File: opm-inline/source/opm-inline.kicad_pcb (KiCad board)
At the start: 4 copper layers, 58 x 40 mm, 71 parts, among them IC1 TMC6200-TA, J1 Info, J2 VCC_IO, J3 PWMx6, J4 Fan, J6 Current Sensing, Q1 HYG025N06LS1C2, Q2 HYG025N06LS1C2, Q3 HYG025N06LS1C2, Q4 HYG025N06LS1C2, Q5 HYG025N06LS1C2, Q6 HYG025N06LS1C2, U2 TerminalBlock_2_P5.08mm, U3 TerminalBlock_3_P5.08mm

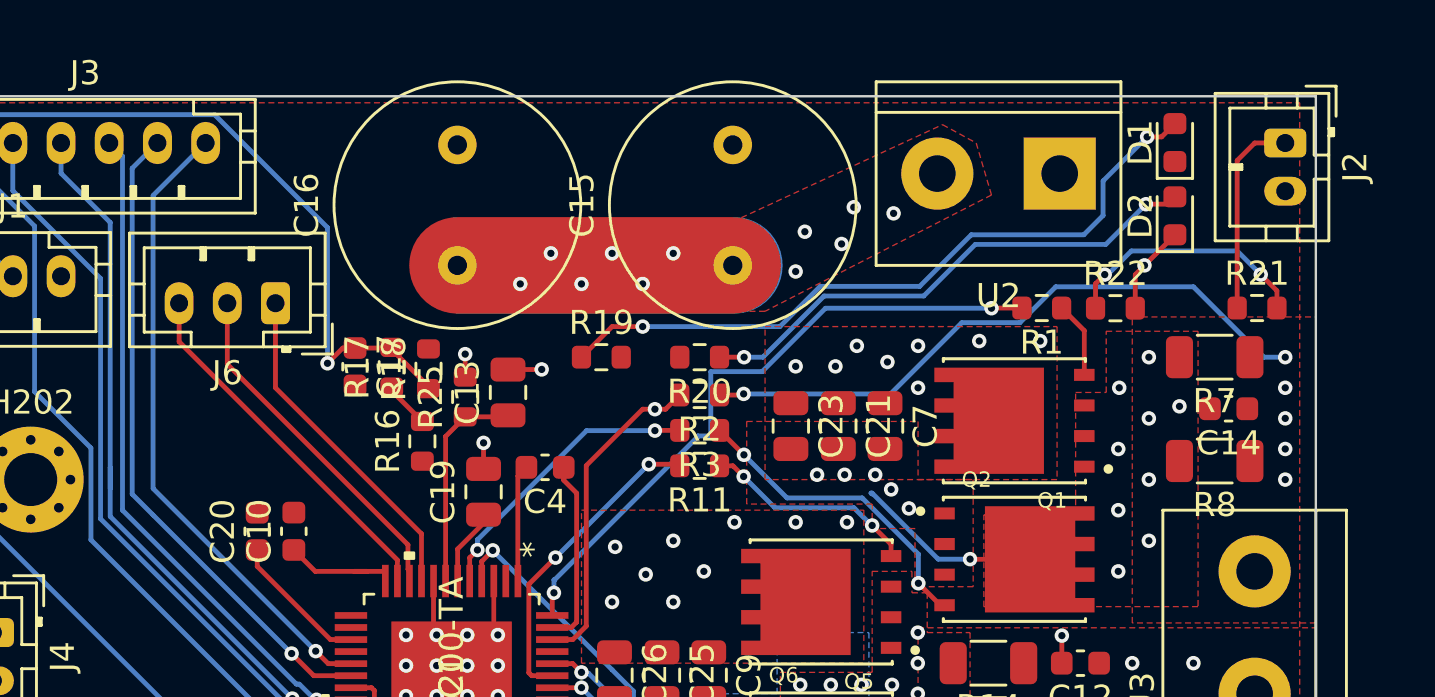
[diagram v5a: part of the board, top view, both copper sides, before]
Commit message: route tracks
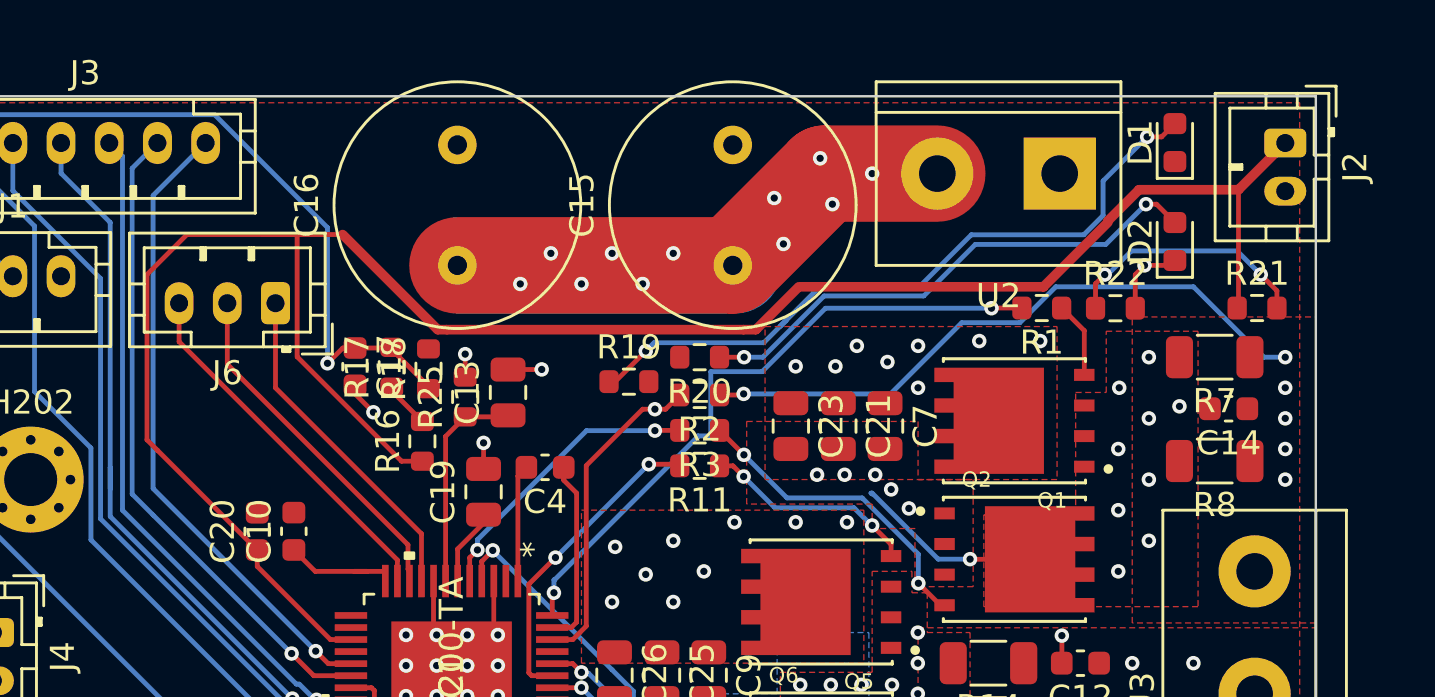
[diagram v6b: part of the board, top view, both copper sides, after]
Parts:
- moved R19 1.53 mm to (159.4, 78.5)
- moved D2 1.07 mm to (182.1, 72.7)
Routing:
- net /+VCC_IO: track 25.9 -> 102.5 mm
- net /+VM: track 71.2 -> 81.3 mm
- net GND: track 23.1 -> 24.1 mm, vias 32 -> 33
- net Net-(D1-Pad2): track 29.7 -> 29.1 mm

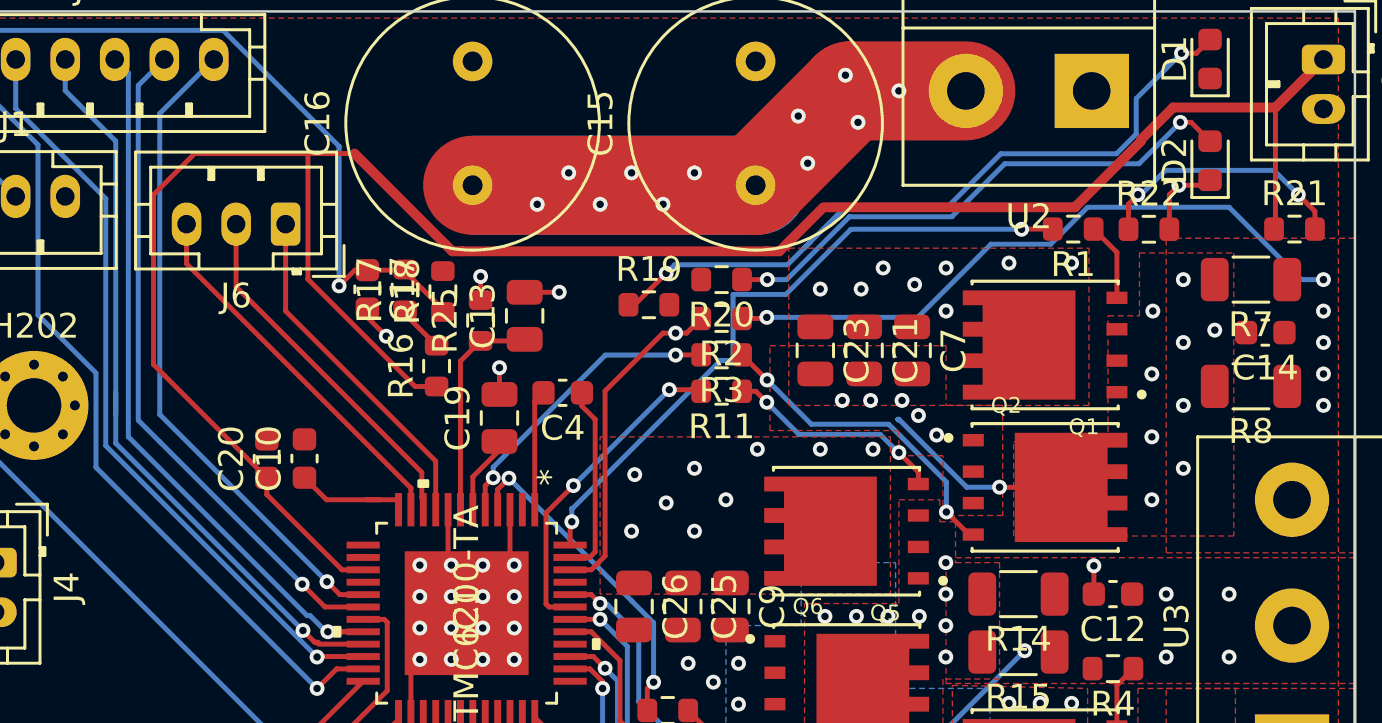
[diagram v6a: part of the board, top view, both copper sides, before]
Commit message: route tracks
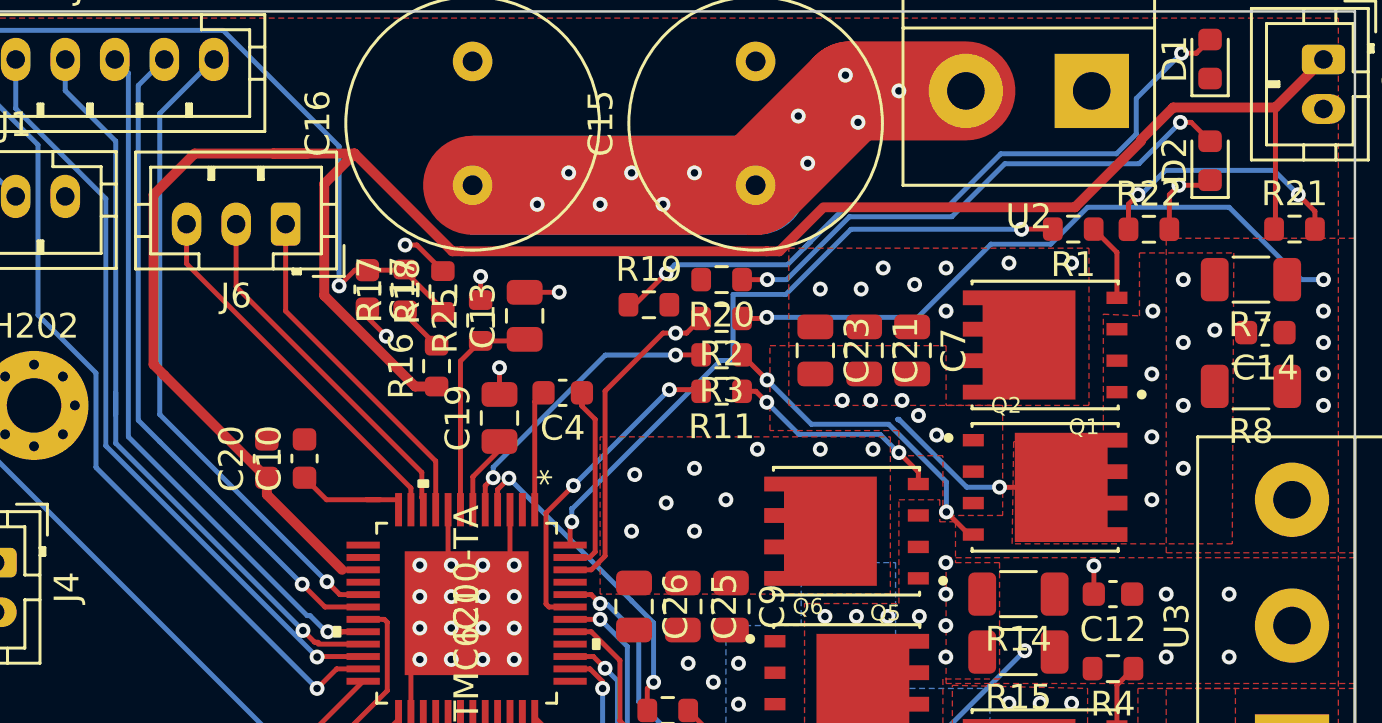
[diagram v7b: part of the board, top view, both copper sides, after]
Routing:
- net GND: track 24.1 -> 26.1 mm, vias 33 -> 34
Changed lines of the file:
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@@
     (thickness 1.6)
     (drawings 4)
-    (tracks 518)
+    (tracks 522)
     (zones 0)
     (modules 71)
@@
   (gr_line (start 187.96 66.64) (end 187.96 106.63) (layer Edge.Cuts) (width 0.1))
   (gr_line (start 187.96 106.63) (end 130.01 106.63) (layer Edge.Cuts) (width 0.1))
+  (via (at 149.606 76.073) (size 0.6) (drill 0.3) (layers F.Cu B.Cu) (net 5))
   (via (at 148.844 79.756) (size 0.6) (drill 0.3) (layers F.Cu B.Cu) (net 5))
   (via (at 185.674 74.041) (size 0.6) (drill 0.3) (layers F.Cu B.Cu) (net 50))
@@
   (segment (start 181.907 73.66) (end 182.11 73.457) (width 0.2) (layer F.Cu) (net 5))
   (segment (start 180.848 73.66) (end 181.907 73.66) (width 0.2) (layer F.Cu) (net 5))
+  (segment (start 150.077 76.073) (end 149.606 76.073) (width 0.2) (layer F.Cu) (net 5))
+  (segment (start 151.13 77.126) (end 150.077 76.073) (width 0.2) (layer F.Cu) (net 5))
   (via (at 146.939 77.724) (size 0.6) (drill 0.3) (layers F.Cu B.Cu) (net 53))
   (via (at 174.498 75.438) (size 0.6) (drill 0.3) (layers F.Cu B.Cu) (net 39))
@@
   (segment (start 179.197 74.041) (end 179.324 74.041) (width 0.2) (layer B.Cu) (net 50))
   (segment (start 147.9117 89.190001) (end 147.0589 89.190001) (width 0.2) (layer F.Cu) (net 52))
-  (segment (start 144.022 86.153101) (end 144.022 85.476) (width 0.2) (layer F.Cu) (net 52))
-  (segment (start 147.0589 89.190001) (end 144.022 86.153101) (width 0.2) (layer F.Cu) (net 52))
+  (segment (start 144.022 86.153101) (end 144.022 85.476) (width 0.4) (layer F.Cu) (net 52))
+  (segment (start 147.0589 89.190001) (end 144.022 86.153101) (width 0.4) (layer F.Cu) (net 52))
   (segment (start 148.884801 91.3103) (end 148.764501 91.19) (width 0.2) (layer F.Cu) (net 52))
   (segment (start 148.884801 94.069701) (end 148.884801 91.3103) (width 0.2) (layer F.Cu) (net 52))
@@
   (segment (start 145.18999 99.15801) (end 145.18999 97.764512) (width 0.2) (layer F.Cu) (net 52))
   (segment (start 144.272 100.076) (end 145.18999 99.15801) (width 0.2) (layer F.Cu) (net 52))
-  (segment (start 150.012522 81.787) (end 150.876 81.787) (width 0.2) (layer F.Cu) (net 52))
-  (segment (start 145.68001 77.454488) (end 150.012522 81.787) (width 0.2) (layer F.Cu) (net 52))
-  (segment (start 145.68001 72.37899) (end 145.68001 77.454488) (width 0.2) (layer F.Cu) (net 52))
-  (segment (start 139.87999 81.33399) (end 144.022 85.476) (width 0.2) (layer F.Cu) (net 52))
-  (segment (start 139.446 80.9) (end 139.87999 81.33399) (width 0.2) (layer F.Cu) (net 52))
-  (segment (start 139.446 74.041) (end 139.446 80.9) (width 0.2) (layer F.Cu) (net 52))
-  (segment (start 141.10801 72.37899) (end 139.446 74.041) (width 0.2) (layer F.Cu) (net 52))
+  (segment (start 139.87999 81.33399) (end 144.022 85.476) (width 0.4) (layer F.Cu) (net 52))
+  (segment (start 139.446 80.9) (end 139.87999 81.33399) (width 0.4) (layer F.Cu) (net 52))
+  (segment (start 139.446 74.041) (end 139.446 80.9) (width 0.4) (layer F.Cu) (net 52))
+  (segment (start 141.10801 72.37899) (end 139.446 74.041) (width 0.4) (layer F.Cu) (net 52))
   (segment (start 176.657 74.549) (end 166.624 74.549) (width 0.4) (layer F.Cu) (net 52))
   (segment (start 179.324 71.882) (end 176.657 74.549) (width 0.4) (layer F.Cu) (net 52))
@@
   (segment (start 184.750001 70.519999) (end 180.621999 70.519999) (width 0.4) (layer F.Cu) (net 52))
   (segment (start 186.69 68.58) (end 184.750001 70.519999) (width 0.4) (layer F.Cu) (net 52))
-  (segment (start 144.28301 72.37899) (end 141.10801 72.37899) (width 0.2) (layer F.Cu) (net 52))
+  (segment (start 144.28301 72.37899) (end 141.10801 72.37899) (width 0.4) (layer F.Cu) (net 52))
   (segment (start 179.324 71.817998) (end 179.324 71.882) (width 0.2) (layer F.Cu) (net 52))
-  (segment (start 145.68001 72.37899) (end 144.28301 72.37899) (width 0.2) (layer F.Cu) (net 52))
+  (segment (start 145.68001 72.37899) (end 144.28301 72.37899) (width 0.4) (layer F.Cu) (net 52))
   (segment (start 184.750001 75.374999) (end 184.695 75.43) (width 0.2) (layer F.Cu) (net 52))
   (segment (start 184.750001 70.519999) (end 184.750001 75.374999) (width 0.2) (layer F.Cu) (net 52))
@@
   (segment (start 166.624 74.549) (end 166.497 74.549) (width 0.2) (layer F.Cu) (net 52))
   (segment (start 164.64688 76.327) (end 164.211 76.327) (width 0.2) (layer F.Cu) (net 52))
-  (segment (start 147.565112 72.37899) (end 144.28301 72.37899) (width 0.2) (layer F.Cu) (net 52))
+  (segment (start 147.565112 72.37899) (end 144.28301 72.37899) (width 0.4) (layer F.Cu) (net 52))
   (segment (start 151.513122 76.327) (end 147.565112 72.37899) (width 0.4) (layer F.Cu) (net 52))
   (segment (start 151.892 76.327) (end 151.513122 76.327) (width 0.4) (layer F.Cu) (net 52))
+  (segment (start 146.338999 73.605103) (end 147.565112 72.37899) (width 0.4) (layer F.Cu) (net 52))
+  (segment (start 146.338999 78.113477) (end 146.338999 73.605103) (width 0.4) (layer F.Cu) (net 52))
+  (segment (start 150.012522 81.787) (end 146.338999 78.113477) (width 0.4) (layer F.Cu) (net 52))
+  (segment (start 150.876 81.787) (end 150.012522 81.787) (width 0.4) (layer F.Cu) (net 52))
   (segment (start 149.579 77.089) (end 149.606 77.062) (width 0.2) (layer F.Cu) (net 53))
   (segment (start 148.082 77.089) (end 149.579 77.089) (width 0.2) (layer F.Cu) (net 53))
@@
     (polygon
       (pts
-        (xy 183.07 87.823364) (xy 174.18 87.823364) (xy 174.18 84.013364) (xy 177.99 84.013364) (xy 177.99 78.933364)
+        (xy 183.007 88.138) (xy 174.117 88.138) (xy 174.18 84.013364) (xy 177.8 83.947) (xy 177.8 78.867)
         (xy 179.26 78.933364) (xy 179.26 76.393364) (xy 183.07 76.393364)
       )

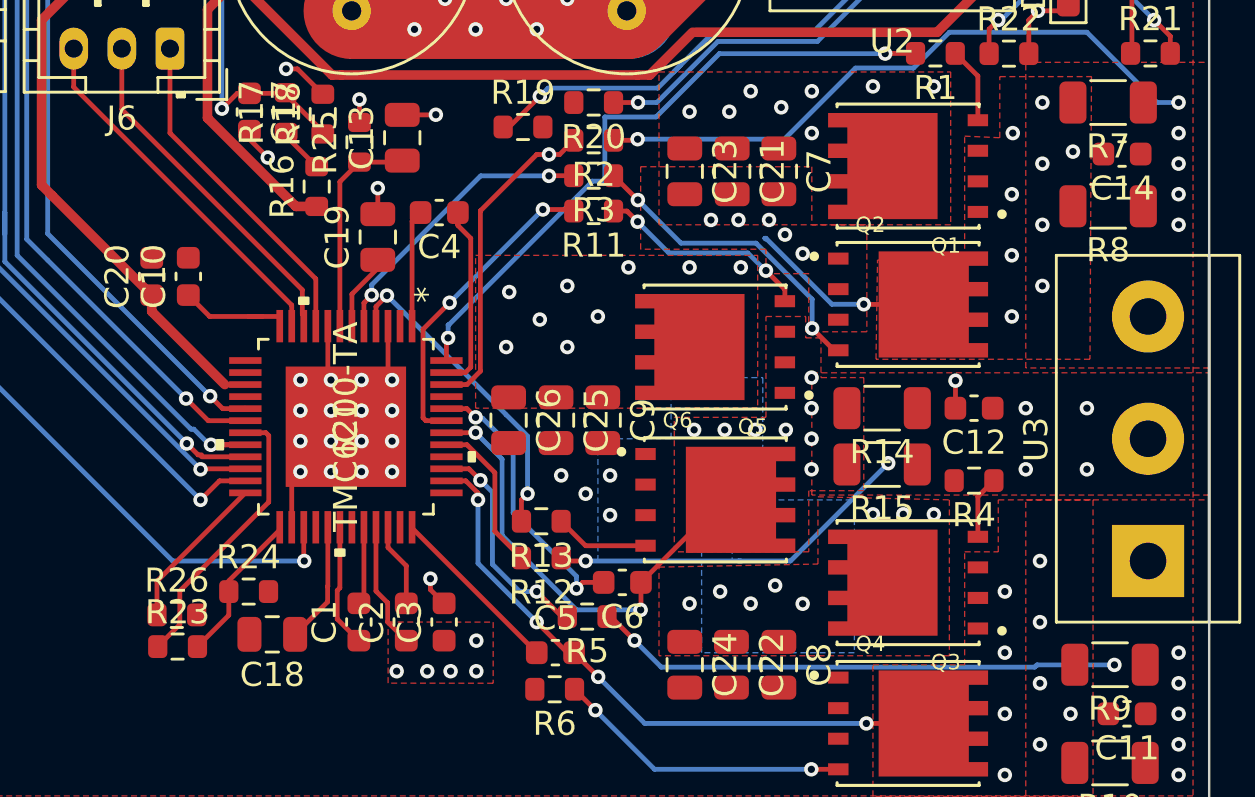
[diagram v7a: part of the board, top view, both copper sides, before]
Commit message: route tracks
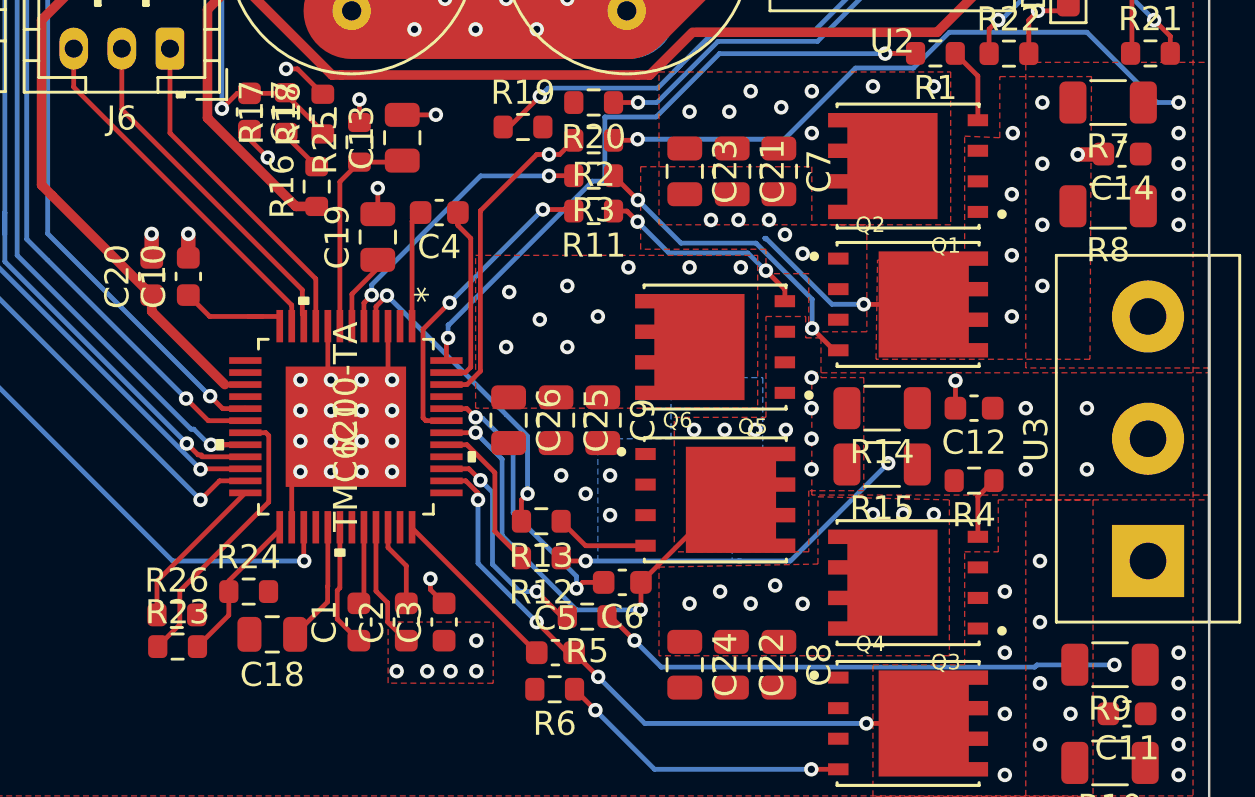
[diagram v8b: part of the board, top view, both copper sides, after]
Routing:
- net GND: track 26.1 -> 29.1 mm, vias 34 -> 36
- removed copper zone on B.Cu, net /+VM
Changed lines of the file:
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@@
     (thickness 1.6)
     (drawings 4)
-    (tracks 522)
+    (tracks 529)
     (zones 0)
     (modules 71)
@@
   (via (at 150.2 92.81) (size 0.6) (drill 0.3) (layers F.Cu B.Cu) (net 5))
   (via (at 182.2 102.87) (size 0.6) (drill 0.3) (layers F.Cu B.Cu) (net 5))
-  (via (at 182.3 79.51) (size 0.6) (drill 0.3) (layers F.Cu B.Cu) (net 5))
+  (via (at 182.499 79.629) (size 0.6) (drill 0.3) (layers F.Cu B.Cu) (net 5))
   (via (at 155.602 97.255) (size 0.6) (drill 0.3) (layers F.Cu B.Cu) (net 5))
   (via (at 160.02 97.79) (size 0.6) (drill 0.3) (layers F.Cu B.Cu) (net 35))
@@
   (segment (start 150.077 76.073) (end 149.606 76.073) (width 0.2) (layer F.Cu) (net 5))
   (segment (start 151.13 77.126) (end 150.077 76.073) (width 0.2) (layer F.Cu) (net 5))
+  (via (at 145.542 82.931) (size 0.6) (drill 0.3) (layers F.Cu B.Cu) (net 5))
+  (via (at 144.018 82.931) (size 0.6) (drill 0.3) (layers F.Cu B.Cu) (net 5))
+  (segment (start 144.018 83.922) (end 144.022 83.926) (width 0.2) (layer F.Cu) (net 5))
+  (segment (start 144.018 82.931) (end 144.018 83.922) (width 0.6) (layer F.Cu) (net 5))
+  (segment (start 145.542 82.931) (end 145.542 83.921) (width 0.6) (layer F.Cu) (net 5))
+  (segment (start 183.546 79.629) (end 183.565 79.61) (width 0.2) (layer F.Cu) (net 5))
+  (segment (start 182.499 79.629) (end 183.546 79.629) (width 0.6) (layer F.Cu) (net 5))
   (via (at 146.939 77.724) (size 0.6) (drill 0.3) (layers F.Cu B.Cu) (net 53))
   (via (at 174.498 75.438) (size 0.6) (drill 0.3) (layers F.Cu B.Cu) (net 39))
@@
       )
     )
-  )
-  (zone (net 3) (net_name /+VM) (layer B.Cu) (hatch edge 0.508)
-    (priority 2)
-    (connect_pads yes (clearance 0.508))
-    (min_thickness 0.254)
-    (fill yes (arc_segments 32) (thermal_gap 0) (thermal_bridge_width 0.508) (smoothing fillet) (radius 0.4))
-    (polygon
-      (pts
-        (xy 173.22 100.33) (xy 166.87 100.33) (xy 166.87 93.98) (xy 173.22 93.98)
-      )
-    )
